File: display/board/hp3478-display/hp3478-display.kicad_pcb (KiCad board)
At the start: 2 copper layers, 130.2 x 29.8 mm, 230 parts, among them J1 SFV10R-1ST, U1 FT60F1x2, U2 SM16206

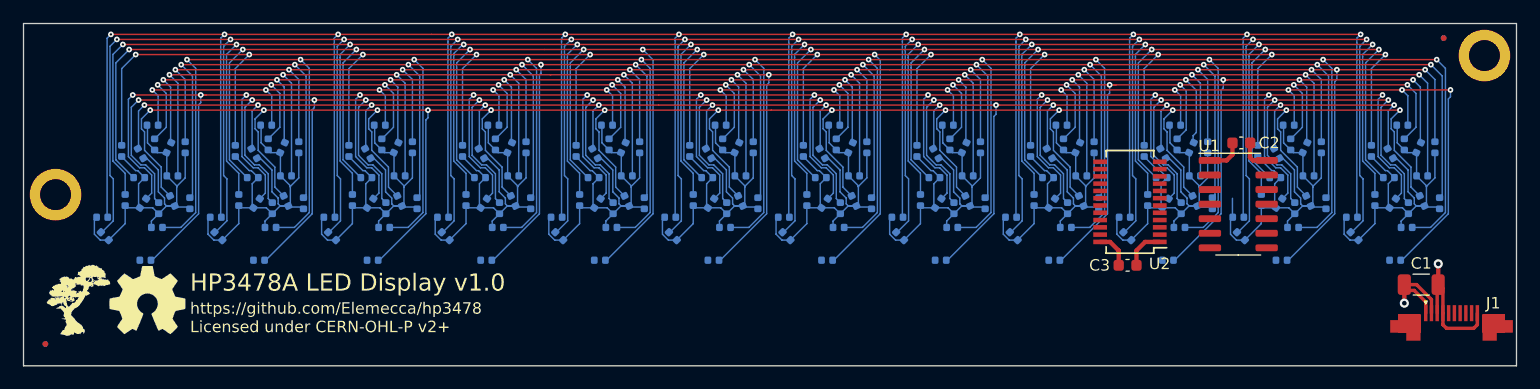
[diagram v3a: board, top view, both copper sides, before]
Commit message: Add missing colon segment and adjust scan matrix.
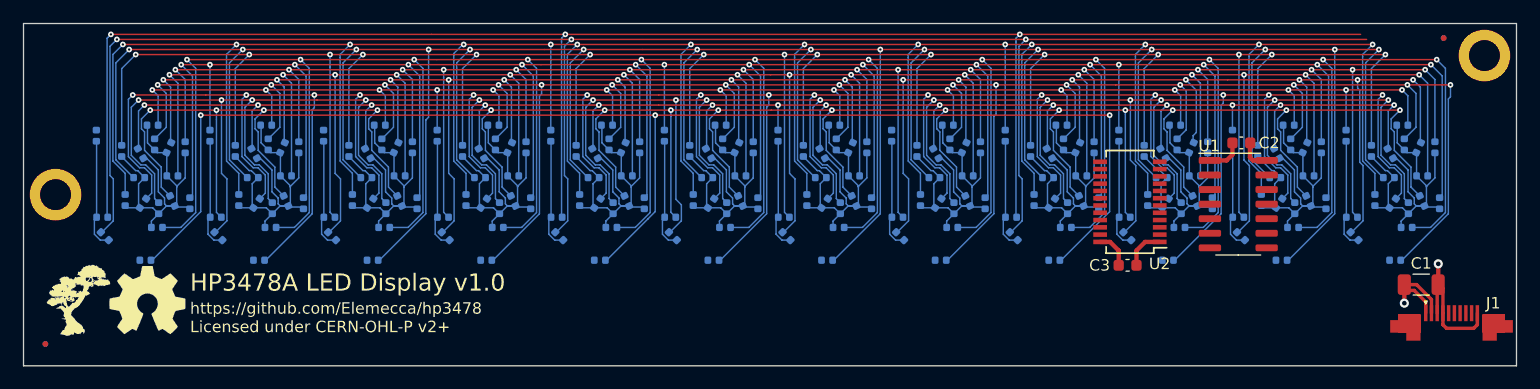
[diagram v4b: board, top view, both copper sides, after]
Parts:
- added D101: LED, 0Local:LED_0402_1005Metric, B.Cu at (191.5, 60.6)
- added D105: LED, 0Local:LED_0402_1005Metric, B.Cu at (181.6, 60.6)
- added D109: LED, 0Local:LED_0402_1005Metric, B.Cu at (171.7, 60.6)
- added D113: LED, 0Local:LED_0402_1005Metric, B.Cu at (161.8, 60.6)
- added D117: LED, 0Local:LED_0402_1005Metric, B.Cu at (151.9, 60.6)
- added D121: LED, 0Local:LED_0402_1005Metric, B.Cu at (142.0, 60.6)
- added D125: LED, 0Local:LED_0402_1005Metric, B.Cu at (132.1, 60.6)
- added D129: LED, 0Local:LED_0402_1005Metric, B.Cu at (122.2, 60.6)
- added D133: LED, 0Local:LED_0402_1005Metric, B.Cu at (112.3, 60.6)
- added D137: LED, 0Local:LED_0402_1005Metric, B.Cu at (102.4, 60.6)
- added D141: LED, 0Local:LED_0402_1005Metric, B.Cu at (92.5, 60.6)
- added D145: LED, 0Local:LED_0402_1005Metric, B.Cu at (82.5, 60.6)
- renumbered D215 to D102, D216 to D103, D101 to D104, D315 to D106, D316 to D107, D102 to D108, D415 to D110, D416 to D111, D103 to D112, D515 to D114, D516 to D115, D104 to D116, D615 to D118, D616 to D119, D105 to D120, D715 to D122, D716 to D123, D106 to D124, D815 to D126, D816 to D127, D107 to D128, D915 to D130, D916 to D131, D108 to D132, D1015 to D134, D1016 to D135, D109 to D136, D1115 to D138, D1116 to D139, D110 to D140, D1215 to D142, D1216 to D143, D111 to D144, D1315 to D146, D1316 to D147, D112 to D148
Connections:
- D102 pad 1: /K0 -> /K12
- D102 pad 2: /A14 -> /A1
- D103 pad 1: /K0 -> /K12
- D103 pad 2: /A15 -> /A2
- D104 pad 2: /A0 -> /A3
- D106 pad 1: /K1 -> /K12
- D106 pad 2: /A14 -> /A5
- D107 pad 1: /K1 -> /K12
- D107 pad 2: /A15 -> /A6
- D108 pad 2: /A1 -> /A7
- D110 pad 1: /K2 -> /K12
- D110 pad 2: /A14 -> /A9
- D111 pad 1: /K2 -> /K12
- D111 pad 2: /A15 -> /A10
- D112 pad 2: /A2 -> /A11
- D114 pad 1: /K3 -> /K12
- D114 pad 2: /A14 -> /A13
- D115 pad 1: /K3 -> /K12
- D115 pad 2: /A15 -> /A14
- D116 pad 2: /A3 -> /A15
- D118 pad 1: /K4 -> /K13
- D118 pad 2: /A14 -> /A1
- D119 pad 1: /K4 -> /K13
- D119 pad 2: /A15 -> /A2
- D120 pad 1: /K12 -> /K13
- D120 pad 2: /A4 -> /A3
- D122 pad 1: /K5 -> /K13
- D122 pad 2: /A14 -> /A5
- D123 pad 1: /K5 -> /K13
- D123 pad 2: /A15 -> /A6
- D124 pad 1: /K12 -> /K13
- D124 pad 2: /A5 -> /A7
- D126 pad 1: /K6 -> /K13
- D126 pad 2: /A14 -> /A9
- D127 pad 1: /K6 -> /K13
- D127 pad 2: /A15 -> /A10
- D128 pad 1: /K12 -> /K13
- D128 pad 2: /A6 -> /A11
- D130 pad 1: /K7 -> /K13
- D130 pad 2: /A14 -> /A13
- D131 pad 1: /K7 -> /K13
- D131 pad 2: /A15 -> /A14
- D132 pad 1: /K12 -> /K13
- D132 pad 2: /A7 -> /A15
- D134 pad 1: /K8 -> /K14
- D134 pad 2: /A14 -> /A1
- D135 pad 1: /K8 -> /K14
- D135 pad 2: /A15 -> /A2
- D136 pad 1: /K12 -> /K14
- D136 pad 2: /A8 -> /A3
- D138 pad 1: /K9 -> /K14
- D138 pad 2: /A14 -> /A5
- D139 pad 1: /K9 -> /K14
- D139 pad 2: /A15 -> /A6
- D140 pad 1: /K12 -> /K14
- D140 pad 2: /A9 -> /A7
- D142 pad 1: /K10 -> /K14
- D142 pad 2: /A14 -> /A9
- D143 pad 1: /K10 -> /K14
- D143 pad 2: /A15 -> /A10
- D144 pad 1: /K12 -> /K14
- D144 pad 2: /A10 -> /A11
- D146 pad 1: /K11 -> /K14
- D146 pad 2: /A14 -> /A13
- D147 pad 1: /K11 -> /K14
- D147 pad 2: /A15 -> /A14
- D148 pad 1: /K12 -> /K14
- D148 pad 2: /A11 -> /A15
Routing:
- net /A15: track 321.1 -> 122.8 mm, vias 12 -> 3
- net /A13: track 314.0 -> 471.2 mm, vias 12 -> 15
- net /A14: track 302.2 -> 162.0 mm, vias 12 -> 3
- net /A7: track 277.0 -> 317.0 mm, vias 13 -> 15
- net /K14: track 0.00 -> 38.6 mm
- net /K13: track 0.00 -> 38.6 mm
- net /K12: track 0.00 -> 38.4 mm
- net /A3: track 191.8 -> 229.3 mm, vias 13 -> 15
- net /A11: track 251.6 -> 283.7 mm, vias 13 -> 15
- net /A6: track 236.6 -> 261.7 mm, vias 13 -> 15
- net /A2: track 196.2 -> 220.2 mm, vias 13 -> 15
- net /A5: track 230.0 -> 253.1 mm, vias 13 -> 15
- net /A10: track 250.4 -> 271.0 mm, vias 13 -> 15
- net /A1: track 207.3 -> 227.7 mm, vias 13 -> 15
- net /A12: track 275.6 -> 290.5 mm, vias 12 -> 14
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
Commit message: Improve workflow for getting digit shapes into KiCAD.
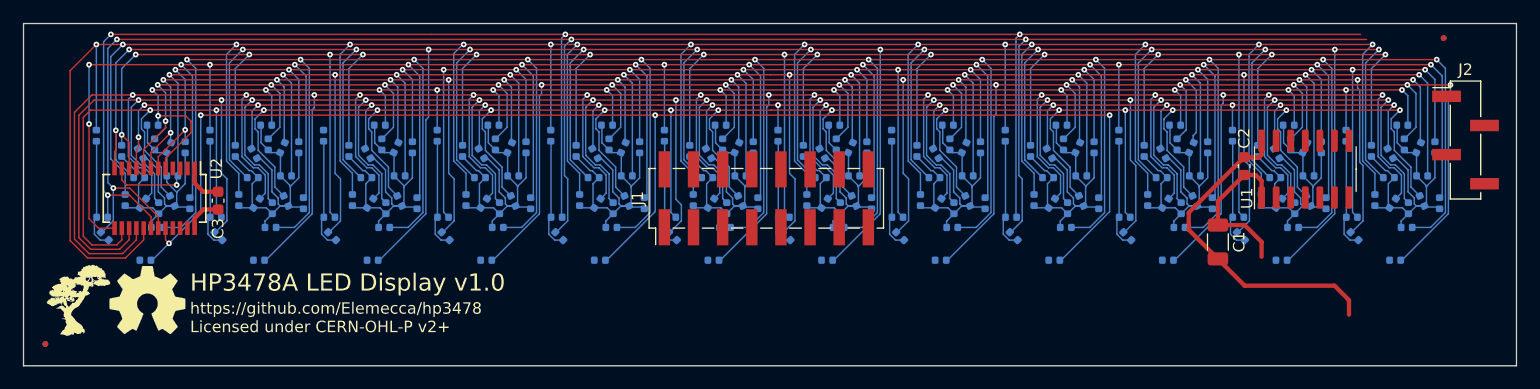
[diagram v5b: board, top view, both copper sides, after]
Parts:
- removed MH1, MH2: MountingHole_2.7mm_M2.5_ISO14580_Pad, MountingHole:MountingHole_2.7mm_M2.5_ISO14580_Pad
- added J2: Header, Connector_PinHeader_2.54mm:PinHeader_1x04_P2.54mm_Vertical_SMD_Pin1Left, F.Cu at (201.9, 61.0)
- J1: value SFV10R-1ST -> Header; footprint 0Local:Amphenol_SFV10R-1ST -> Connector_PinHeader_2.54mm:PinHeader_2x08_P2.54mm_Vertical_SMD
- moved U2 85.0 mm to (87.6, 66.0), turned to -90 degrees
- moved C3 79.5 mm to (93.2, 66.2), turned to 90 degrees
- moved J1 60.9 mm to (141.0, 66.0), turned to 90 degrees
- moved C1 18.1 mm to (180.3, 69.8), turned to -90 degrees
- moved U1 6.59 mm to (188.0, 63.5), turned to 90 degrees
- moved C2 2.03 mm to (182.6, 63.2), turned to 90 degrees
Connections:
- net /HSYNC renamed /LCD_SYNC
- J1 pad 1: +5V -> /LCD_3V3
- J1 pad 10: GND -> /LCD_IWA
- J1 pad 3: GND -> /LCD_2V2
- J1 pad 4: GND -> /LCD_ISA
- J1 pad 5: /HP1 -> /LCD_1V1
- J1 pad 7: /HISA -> GND
- J1 pad 8: /HIWA -> /LCD_IWB
- J1 pad 9: /HPWO -> /LCD_OS1
- U1 pad 10: /HPWO -> /LCD_PWO
- U1 pad 11: /HP1 -> /LCD_P1
- U1 pad 3: /HIWA -> /LCD_IWA
- U1 pad 4: /HISA -> /LCD_ISA
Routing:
- net /A12: track 290.5 -> 327.2 mm, vias 14 -> 15
- net /A11: track 283.7 -> 307.9 mm
- net /A8: track 271.3 -> 295.3 mm, vias 15 -> 17
- net /A10: track 271.0 -> 293.6 mm
- net /A9: track 243.4 -> 264.8 mm
- net GND: track 18.7 -> 32.5 mm, vias 1 -> 0
- net /A0: track 155.4 -> 163.5 mm, vias 14 -> 15
- net /A6: track 261.7 -> 268.5 mm, vias 15 -> 16
- net /A14: track 162.0 -> 168.1 mm, vias 3 -> 4
- net /A13: track 471.2 -> 477.0 mm, vias 15 -> 16
- net /A3: track 229.3 -> 234.2 mm, vias 15 -> 16
- net /A1: track 227.7 -> 232.0 mm, vias 15 -> 16
- net /A2: track 220.2 -> 224.1 mm, vias 15 -> 16
- net /A7: track 317.0 -> 320.4 mm, vias 15 -> 16
- net /A5: track 253.1 -> 256.3 mm, vias 15 -> 16
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
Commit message: Clean up some routing.
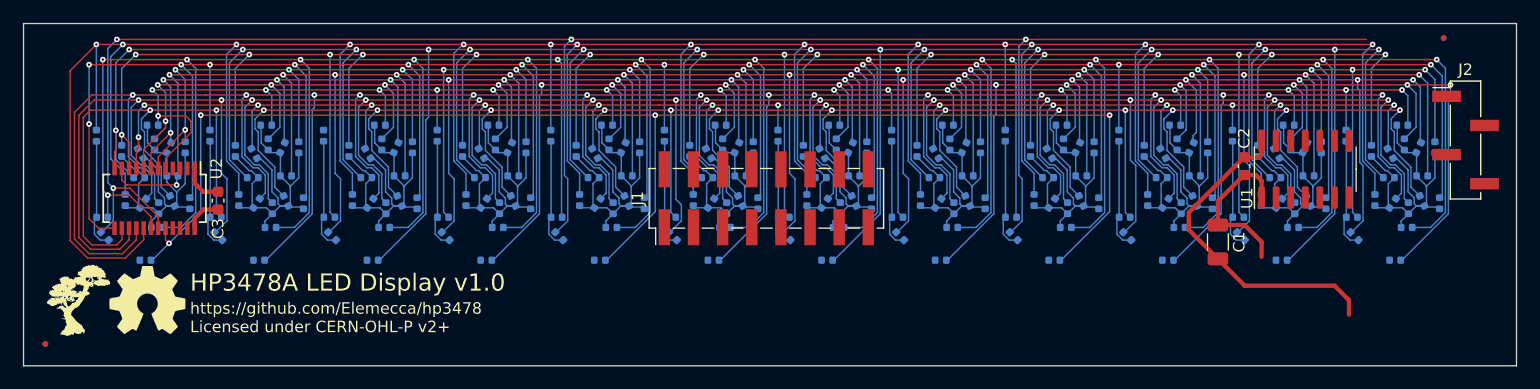
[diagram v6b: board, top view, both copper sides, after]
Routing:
- net /A13: track 477.0 -> 368.6 mm
- net /A0: track 163.5 -> 167.1 mm, vias 15 -> 16
